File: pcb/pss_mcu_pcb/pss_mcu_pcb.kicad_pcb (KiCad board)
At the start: 2 copper layers, 30.1 x 40.1 mm, 50 parts, among them J1 STM32_Prog, J2 UART_Prog, J3 Conn_01x18, J4 Conn_01x18, SW1 Boot, SW2 EN, SW3 SW_Push, U1 LM3940IMP-3.3_NOPB, U2 LM358, U3 STM32F030K6Tx, U4 ESP32-WROOM-32U

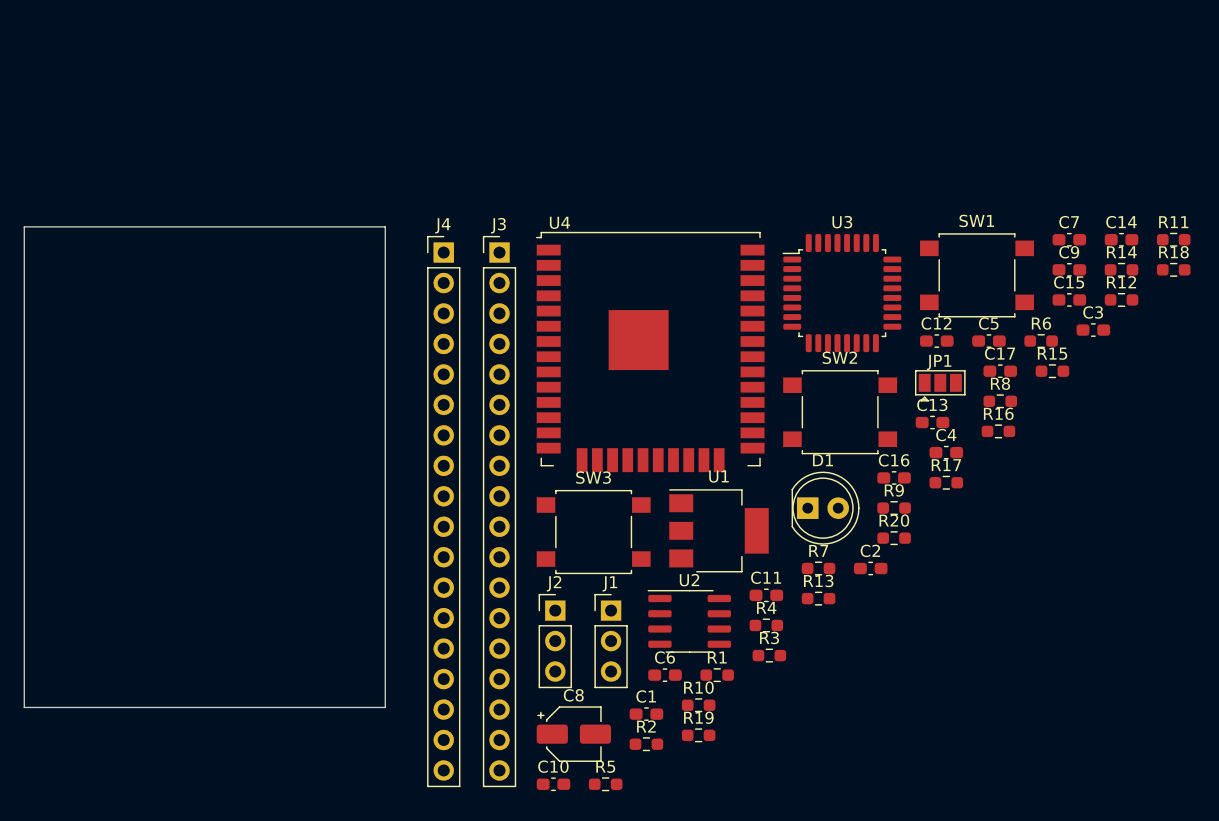
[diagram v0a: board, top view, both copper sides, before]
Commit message: Change elements placement
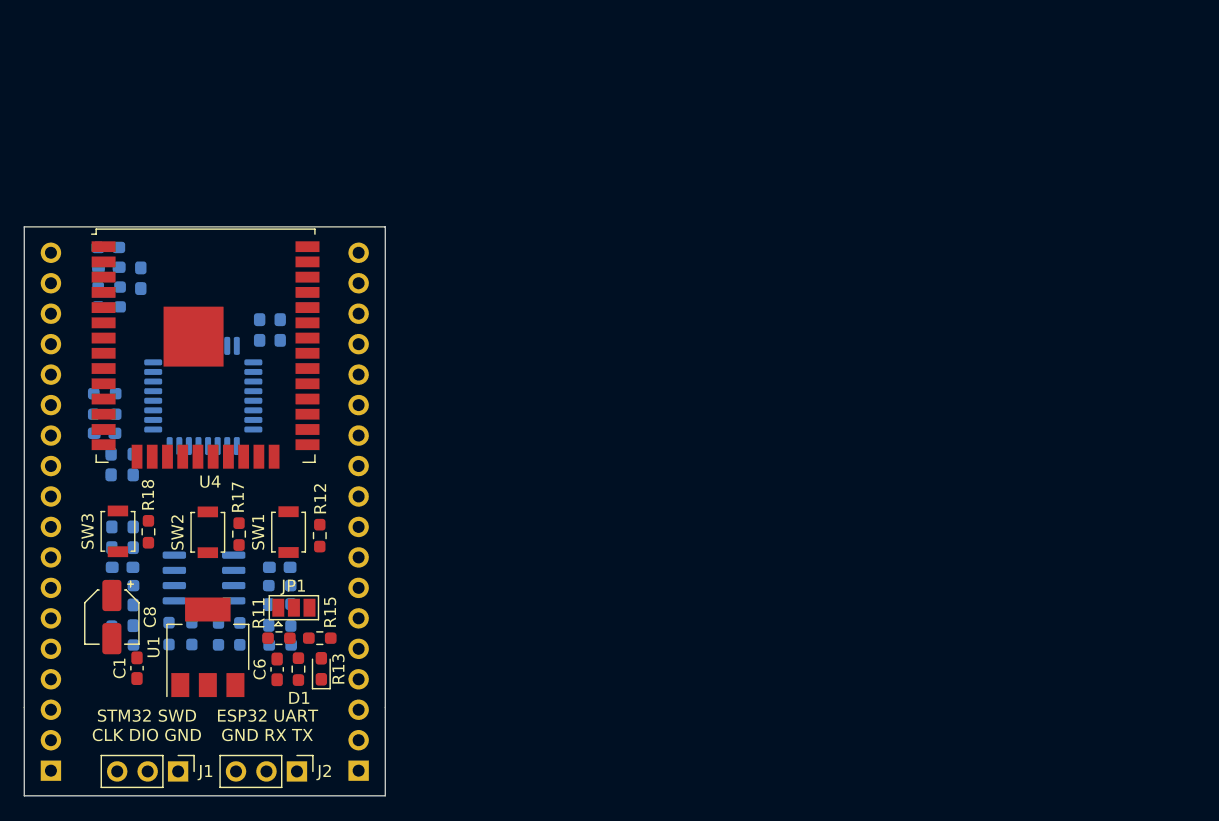
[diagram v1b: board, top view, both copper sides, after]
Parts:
- C10, C11, C12, C13, C14, C15, C16, C17, C2, C3, C4, C5, C7, C9, J3, J4, R1, R10, R14, R16, R19, R2, R20, R3, R4, R5, R6, R7, R8, R9, U2, U3: moved to B.Cu
- D1: footprint LED_THT:LED_D5.0mm -> LED_SMD:LED_0603_1608Metric_Pad1.05x0.95mm_HandSolder
- SW1, SW2, SW3: footprint Button_Switch_SMD:SW_SPST_B3S-1000 -> Button_Switch_SMD:SW_SPST_B3U-1000P
- moved R18 88.2 mm to (121.5, 109.2), turned to 90 degrees
- moved C14 84.5 mm to (120.2, 103.6), turned to 270 degrees
- moved R14 84.4 mm to (118.2, 88.8), turned to 180 degrees
- moved C3 82.4 mm to (118.1, 85.5)
- moved C7 81.9 mm to (120.2, 109.7), turned to 90 degrees
- moved R11 81.7 mm to (132.4, 118.1)
- moved C9 81.5 mm to (118.4, 103.6), turned to 270 degrees
- moved R6 80.7 mm to (119.3, 118.7)
- moved R8 76.2 mm to (118.4, 116.2), turned to 270 degrees
- moved R16 74.9 mm to (118.2, 90.5), turned to 180 degrees
- moved C5 73.6 mm to (118.2, 87.2)
- moved C17 72.1 mm to (120.8, 88.1), turned to 90 degrees
- moved C12 69.8 mm to (117.8, 101.0), turned to 180 degrees
- moved R12 69.7 mm to (135.8, 109.6), turned to 90 degrees
- moved C15 69.5 mm to (132.4, 112.2), turned to 180 degrees
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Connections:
- J3 pad 10: DISP_T_CS -> DISP_CS
- J3 pad 14: SD_CS -> SD_SDO
- J3 pad 16: SD_SDO -> SD_SCK
- J3 pad 17: SD_SCK -> SD_CS
- J3 pad 3: DISP_CS -> DISP_T_CS
- J3 pad 4: DISP_RST -> DISP_T_CLK
- J3 pad 5: DISP_DC_RS -> DISP_SDO
- J3 pad 6: DISP_SDI -> DISP_SCK
- J3 pad 7: DISP_SCK -> DISP_SDI
- J3 pad 8: DISP_SDO -> DISP_DC_RS
- J3 pad 9: DISP_T_CLK -> DISP_RST
- J4 pad 10: HotA_Enc_B -> Sold_Enc_B
- J4 pad 11: HotA_Enc_A -> HotA_Switch
- J4 pad 12: Sold_Switch -> Fan_PWM
- J4 pad 13: Sold_Enc_B -> Hot_Air_Reed
- J4 pad 14: Sold_Enc_A -> HotA_Enc_B
- J4 pad 3: Sold_PWM -> Iron_Therm_Pos
- J4 pad 4: Iron_Therm_Pos -> Hot_Air_Therm_Pos
- J4 pad 5: Hot_Air_Therm_Pos -> Sold_PWM
- J4 pad 6: Hot_Air_Reed -> Sold_Switch
- J4 pad 7: Fan_PWM -> Heater_PWM
- J4 pad 8: Heater_PWM -> HotA_Enc_A
- J4 pad 9: HotA_Switch -> Sold_Enc_A
- U3 pad 10: (no net) -> Sold_PWM
- U3 pad 11: (no net) -> Sold_Switch
- U3 pad 12: (no net) -> Heater_PWM
- U3 pad 13: (no net) -> HotA_Enc_A
- U3 pad 15: (no net) -> Hot_Air_Themp_ADC
- U3 pad 20: Sold_Switch -> HotA_Switch
- U3 pad 21: Heater_PWM -> Fan_PWM
- U3 pad 22: (no net) -> Hot_Air_Reed
- U3 pad 26: HotA_Switch -> (no net)
- U3 pad 28: HotA_Enc_A -> (no net)
- U3 pad 29: Fan_PWM -> (no net)
- U3 pad 3: Hot_Air_Reed -> (no net)
- U3 pad 30: Sold_PWM -> (no net)
- U3 pad 6: Iron_Themp_ADC -> (no net)
- U3 pad 7: Hot_Air_Themp_ADC -> Iron_Themp_ADC
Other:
- board size 30.1 x 40.1 mm -> 30.1 x 47.4 mm
- copper layers 2 -> 4
- board text added: "ESP32 UART GND RX TX"
- board text added: "STM32 SWD CLK DIO GND"

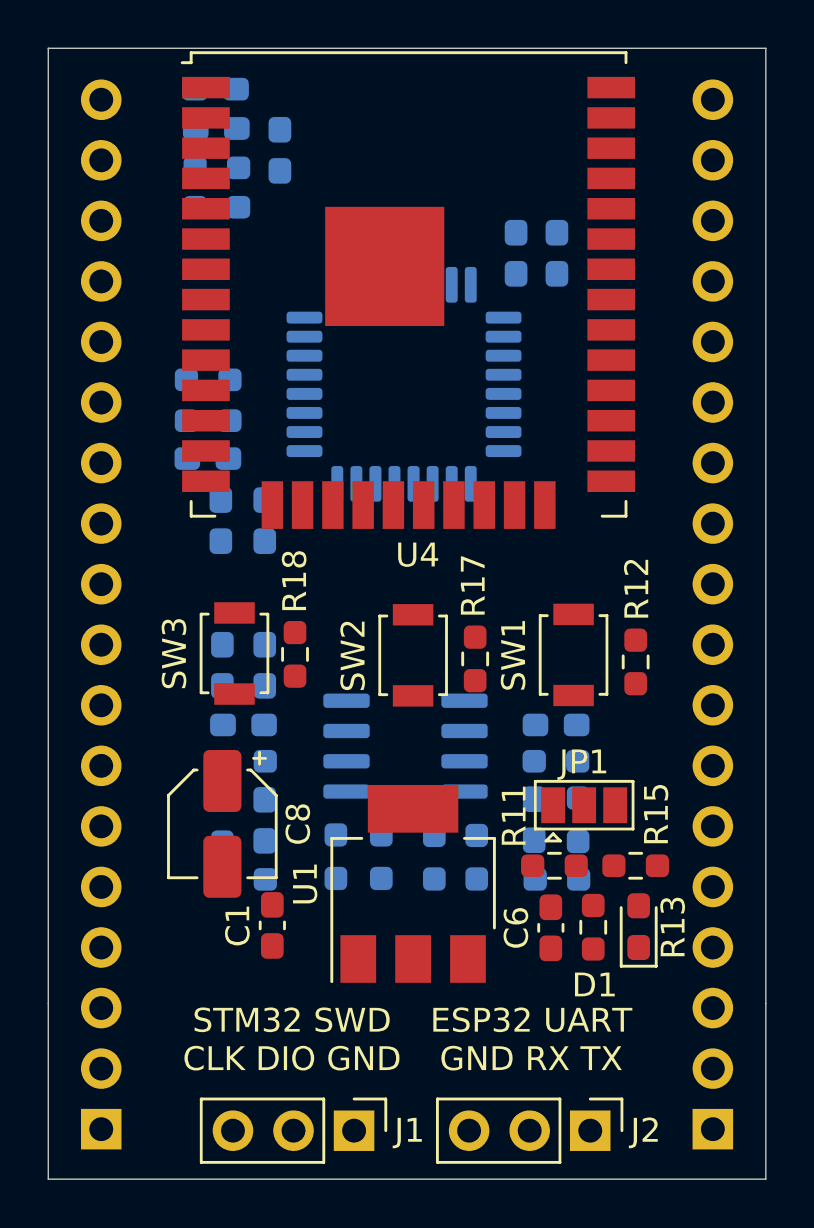
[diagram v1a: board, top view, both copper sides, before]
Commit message: Add new routes
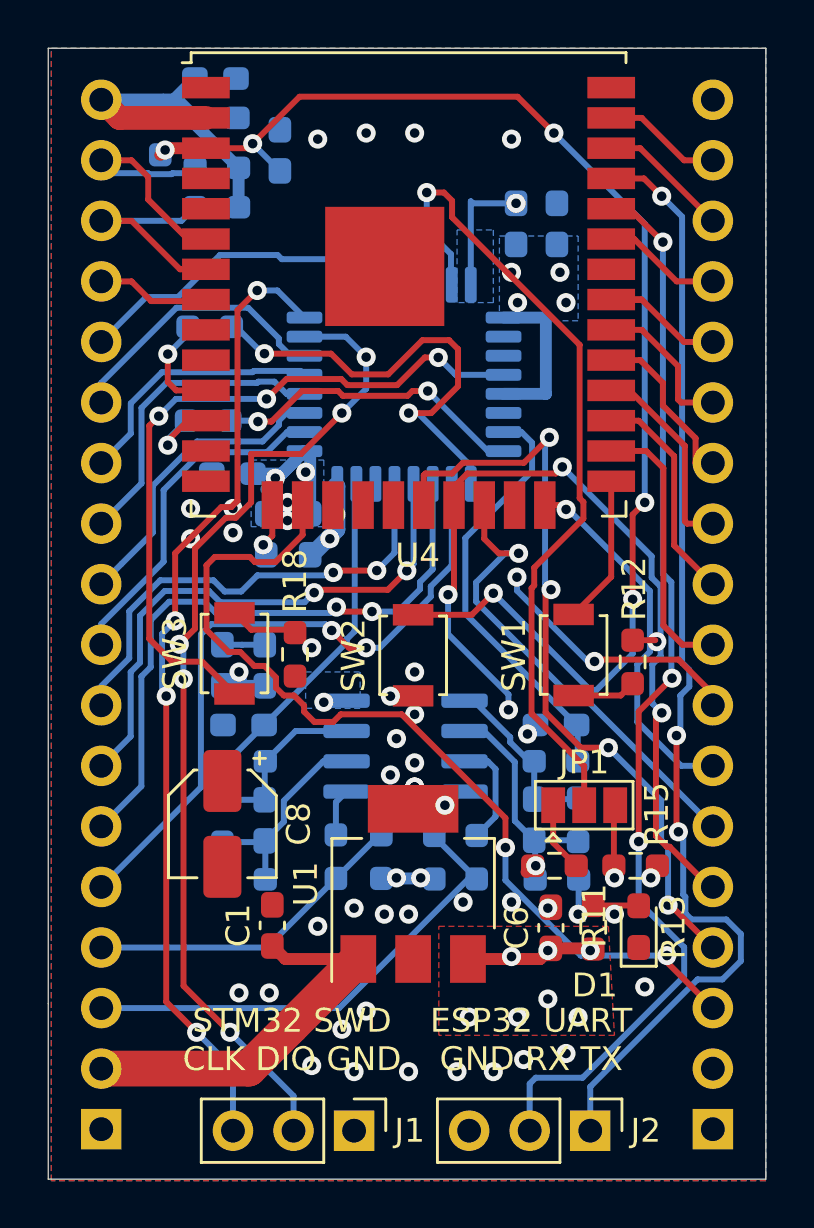
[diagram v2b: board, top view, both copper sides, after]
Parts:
- R17: moved to B.Cu
- moved R17 25.7 mm to (115.8, 87.4), turned to 270 degrees
- moved R19 2.22 mm to (117.9, 95.5)
- moved C14 1.99 mm to (122.1, 104.2)
- moved C9 1.99 mm to (120.3, 104.2)
- moved C2 1.23 mm to (130.7, 91.2)
- moved C4 1.23 mm to (132.5, 91.2)
- moved C12 1.21 mm to (118.8, 101.7)
- moved C5 0.44 mm to (118.2, 86.7)
- moved C3 0.44 mm to (118.1, 85.1)
- moved R12 0.13 mm to (135.6, 109.6)
- turned C16 to 180 degrees
- turned R11 to 180 degrees
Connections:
- J3 pad 10: DISP_CS -> DISP_T_CS
- J3 pad 11: DISP_T_DIN -> DISP_T_CLK
- J3 pad 12: Boot -> DISP_SDO
- J3 pad 13: DISP_T_IRQ -> DISP_SCK
- J3 pad 14: SD_SDO -> DISP_SDI
- J3 pad 15: SD_SDI -> DISP_DC_RS
- J3 pad 16: SD_SCK -> DISP_RST
- J3 pad 17: SD_CS -> DISP_CS
- J3 pad 3: DISP_T_CS -> SD_CS
- J3 pad 4: DISP_T_CLK -> SD_SCK
- J3 pad 5: DISP_SDO -> SD_SDI
- J3 pad 6: DISP_SCK -> SD_SDO
- J3 pad 7: DISP_SDI -> DISP_T_IRQ
- J3 pad 8: DISP_DC_RS -> DISP_T_DO
- J3 pad 9: DISP_RST -> DISP_T_DIN
- J4 pad 10: Sold_Enc_B -> Sold_Enc_A
- J4 pad 9: Sold_Enc_A -> Sold_Enc_B
- U4 pad 23: (no net) -> DISP_T_DO
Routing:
- net EN: track 0.00 -> 55.5 mm, vias 0 -> 6
- net TXD: track 0.00 -> 47.5 mm, vias 0 -> 3
- net RXD: track 0.00 -> 45.4 mm, vias 0 -> 3
- net +3V3: track 0.00 -> 44.2 mm, vias 0 -> 20
- net STM_SWDIO: track 0.00 -> 42.3 mm, vias 0 -> 5
- net STM_SWCLK: track 0.00 -> 40.8 mm, vias 0 -> 4
- net SD_CS: track 0.00 -> 38.9 mm, vias 0 -> 2
- net SD_SDI: track 0.00 -> 36.3 mm, vias 0 -> 4
- net STM_BOOT: track 0.00 -> 35.0 mm, vias 0 -> 1
- net SD_SCK: track 0.00 -> 32.5 mm, vias 0 -> 4
- net STM_RST: track 0.00 -> 30.0 mm, vias 0 -> 3
- net Sold_PWM: track 0.00 -> 28.5 mm, vias 0 -> 2
- net Sold_Switch: track 0.00 -> 26.5 mm, vias 0 -> 2
- net Heater_PWM: track 0.00 -> 23.1 mm, vias 0 -> 2
- net Iron_Therm_Pos: track 0.00 -> 20.6 mm
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- added copper zone on B.Cu, net +3V3
- added copper zone on F.Cu, net +3V3
- added copper zone on In1.Cu, net +3V3
- added copper zone on B.Cu, net GND
- added copper zone on F.Cu, net GND
- added copper zone on In2.Cu, net GND
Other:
- net class Power added: clearance 0.3, trace_width 0.5, via_dia 0.8, via_drill 0.4

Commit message: Fix design issues
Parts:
- moved R16 36.4 mm to (150.4, 73.5)
- moved R14 36.3 mm to (150.4, 71.9)
- moved C5 36.3 mm to (150.3, 69.8)
- moved C3 36.3 mm to (150.4, 68.3)
- moved C17 36.2 mm to (152.8, 71.2)
- moved R17 36.2 mm to (147.9, 70.7)
- moved C1 36.1 mm to (152.5, 103.7)
- moved C10 36.1 mm to (163.4, 99.3)
- moved C2 36.1 mm to (162.7, 74.3)
- moved D1 36.1 mm to (167.8, 103.8)
- moved R11 36.1 mm to (164.3, 101.2)
- moved R12 36.1 mm to (167.6, 92.7)
- moved R2 36.1 mm to (157.0, 100.8)
- moved R5 36.1 mm to (155.1, 100.8)
- moved R7 36.1 mm to (165.3, 99.3)
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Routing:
- net DISP_T_DO: track 11.1 -> 14.1 mm
- net +3V3: track 44.2 -> 46.6 mm, vias 20 -> 22
- net SD_SDO: track 20.0 -> 18.6 mm
- net EN: track 55.5 -> 56.8 mm
- net GND: track 16.7 -> 16.5 mm, vias 49 -> 61

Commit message: Add name
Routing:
- net TXD: track 47.5 -> 44.0 mm
- net EN: track 56.8 -> 54.8 mm
- net SD_SCK: track 32.5 -> 34.1 mm
- net DISP_T_DO: track 14.1 -> 15.2 mm
- net RXD: track 45.5 -> 44.5 mm
- net SD_CS: track 38.9 -> 39.9 mm
- net DISP_T_IRQ: track 15.5 -> 14.6 mm
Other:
- board text added: "PSS_MCU_board rev 0.1 20201122"

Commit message: Add files for manufacturing
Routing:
- net +3V3: track 46.6 -> 59.0 mm, vias 22 -> 13
- net GND: track 16.0 -> 25.2 mm, vias 61 -> 45
- net SD_CS: track 39.9 -> 34.3 mm
- net SD_SDO: track 18.6 -> 20.4 mm
- net Iron_Themp_ADC: track 17.9 -> 19.5 mm
- net EN: track 54.8 -> 53.9 mm
- net STM_SWDIO: track 42.3 -> 41.5 mm
- net DISP_T_DIN: track 11.5 -> 10.8 mm
- net SD_SDI: track 35.9 -> 36.5 mm
